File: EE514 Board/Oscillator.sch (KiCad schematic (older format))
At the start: 13 parts

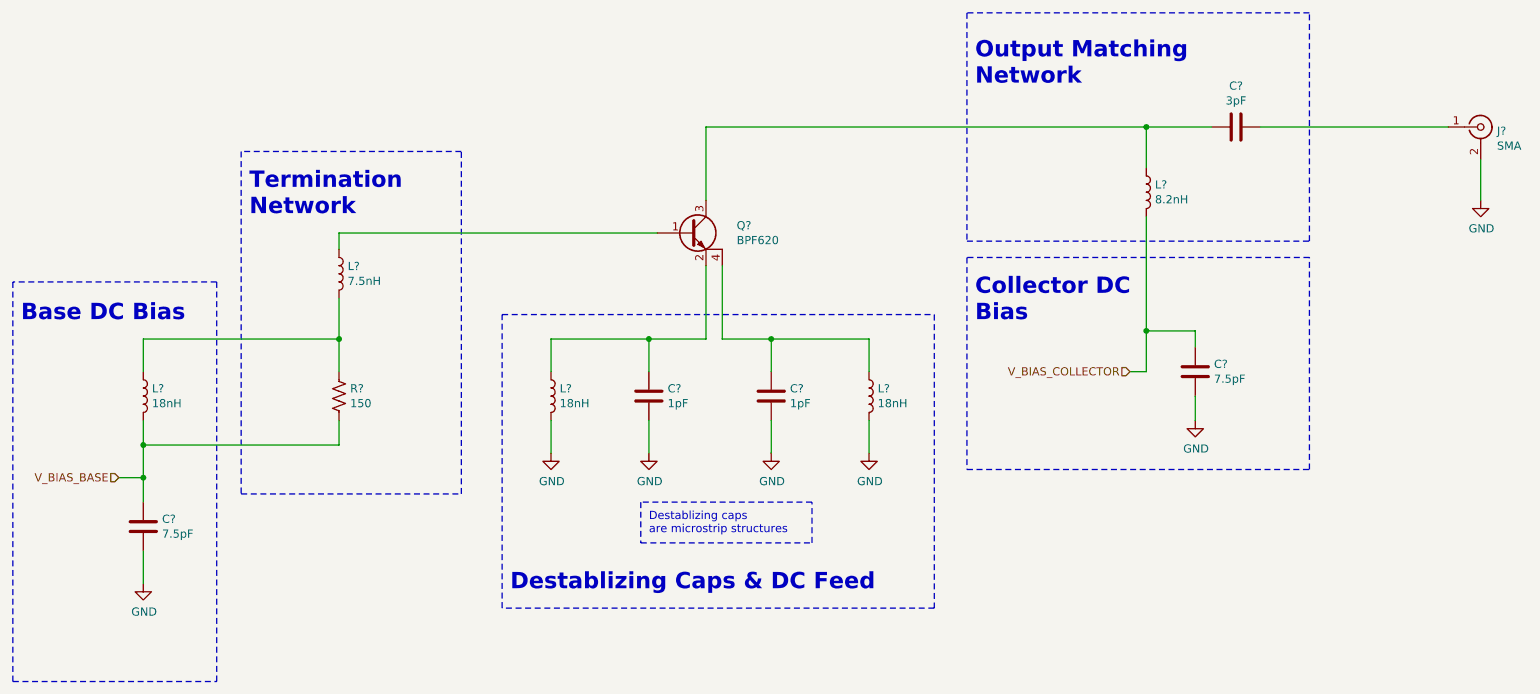
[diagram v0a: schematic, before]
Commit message: Layout finished, updating silkscreen...
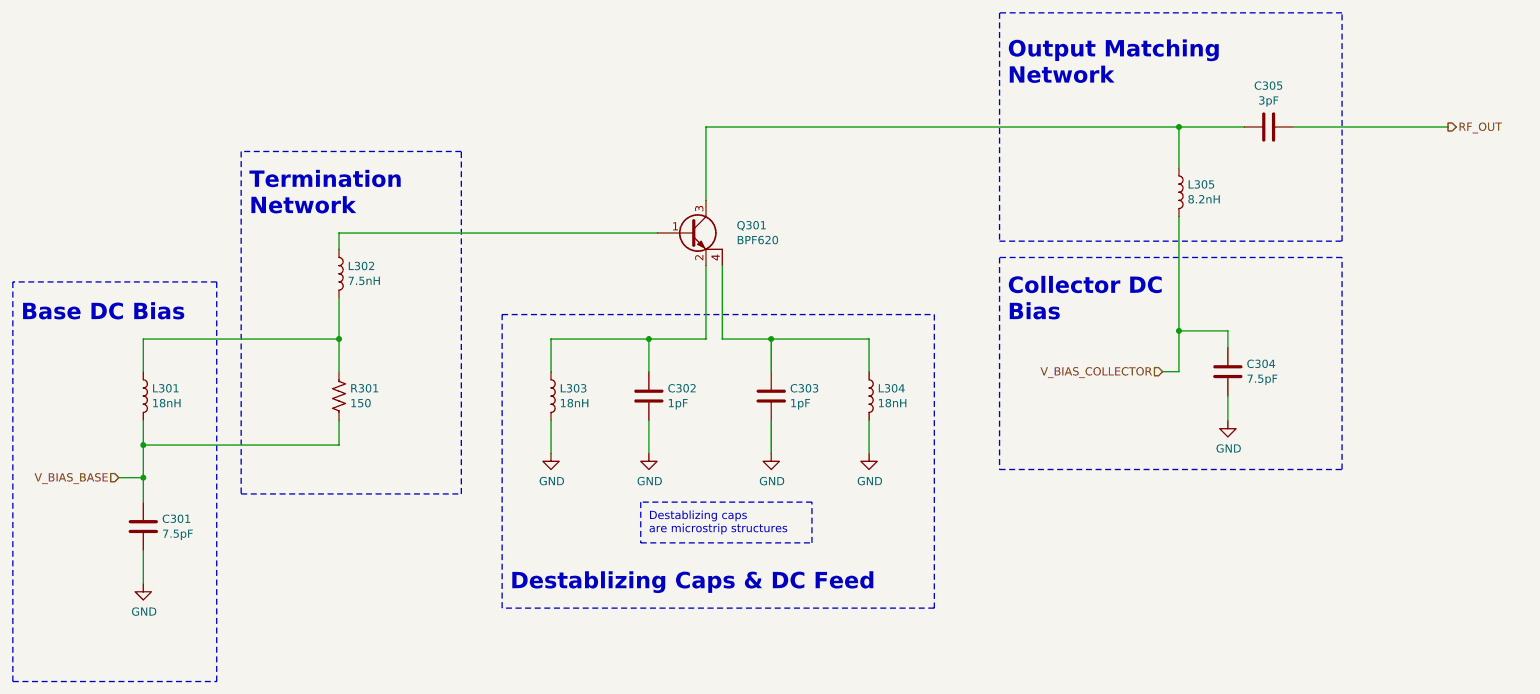
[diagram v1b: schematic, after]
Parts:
- removed J?: SMA, symbol Connector:Conn_Coaxial
- C301, C304, C305: renamed from C?; footprint (none) -> EE514 Board:C_0603_1608Metric_Pad0.98x0.95mm_HandSolder
- C302, C303: renamed from C?; footprint (none) -> EE514 Board:C_1pF_Interdigital
- L301, L302, L303, L304, L305: renamed from L?; footprint (none) -> EE514 Board:L_0603_1608Metric_Pad0.98x0.95mm_HandSolder
- Q301: renamed from Q?; footprint (none) -> EE514 Board:SOT-343_2.0x1.25mm_P1.3mm
- R301: renamed from R?; footprint (none) -> EE514 Board:R_0603_1608Metric_Pad0.98x0.95mm_HandSolder
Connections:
- net RF_OUT: now reaches C305.1
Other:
- moved on the sheet: C304, C305, L305
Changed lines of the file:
@@
 $Descr A4 11693 8268
 encoding utf-8
-Sheet 3 4
+Sheet 3 5
 Title ""
 Date ""
@@
 $EndDescr
 $Comp
-L Device:C C?
+L Device:C C301
 U 1 1 619CBBF5
 P 2250 4900
-F 0 "C?" H 2365 4946 50  0000 L CNN
+F 0 "C301" H 2365 4946 50  0000 L CNN
 F 1 "7.5pF" H 2365 4855 50  0000 L CNN
-F 2 "" H 2288 4750 50  0001 C CNN
+F 2 "EE514 Board:C_0603_1608Metric_Pad0.98x0.95mm_HandSolder" H 2288 4750 50  0001 C CNN
 F 3 "~" H 2250 4900 50  0001 C CNN
 	1    2250 4900
@@
 $EndComp
 $Comp
-L power:GND #PWR?
+L power:GND #PWR0301
 U 1 1 619CC4D1
 P 2250 5250
-F 0 "#PWR?" H 2250 5000 50  0001 C CNN
+F 0 "#PWR0301" H 2250 5000 50  0001 C CNN
 F 1 "GND" H 2255 5077 50  0000 C CNN
 F 2 "" H 2250 5250 50  0001 C CNN
@@
 $EndComp
 $Comp
-L Device:R_US R?
+L Device:R_US R301
 U 1 1 619CCA1F
 P 3450 4100
-F 0 "R?" H 3518 4146 50  0000 L CNN
+F 0 "R301" H 3518 4146 50  0000 L CNN
 F 1 "150" H 3518 4055 50  0000 L CNN
-F 2 "" V 3490 4090 50  0001 C CNN
+F 2 "EE514 Board:R_0603_1608Metric_Pad0.98x0.95mm_HandSolder" V 3490 4090 50  0001 C CNN
 F 3 "~" H 3450 4100 50  0001 C CNN
 	1    3450 4100
@@
 $EndComp
 $Comp
-L EE514_Board:Q_NPN_BECE Q?
+L EE514_Board:Q_NPN_BECE Q301
 U 1 1 619CD2F0
 P 5600 3100
-F 0 "Q?" H 5888 3146 50  0000 L CNN
+F 0 "Q301" H 5888 3146 50  0000 L CNN
 F 1 "BPF620" H 5888 3055 50  0000 L CNN
-F 2 "" H 5800 3200 50  0001 C CNN
+F 2 "EE514 Board:SOT-343_2.0x1.25mm_P1.3mm" H 5800 3200 50  0001 C CNN
 F 3 "~" H 5600 3100 50  0001 C CNN
 	1    5600 3100
@@
 $EndComp
 $Comp
-L Device:L L?
+L Device:L L301
 U 1 1 619CDAD5
 P 2250 4100
-F 0 "L?" H 2303 4146 50  0000 L CNN
+F 0 "L301" H 2303 4146 50  0000 L CNN
 F 1 "18nH" H 2303 4055 50  0000 L CNN
-F 2 "" H 2250 4100 50  0001 C CNN
+F 2 "EE514 Board:L_0603_1608Metric_Pad0.98x0.95mm_HandSolder" H 2250 4100 50  0001 C CNN
 F 3 "~" H 2250 4100 50  0001 C CNN
 	1    2250 4100
@@
 	2250 5250 2250 5050
 $Comp
-L Device:L L?
+L Device:L L302
 U 1 1 619CE6FD
 P 3450 3350
-F 0 "L?" H 3503 3396 50  0000 L CNN
+F 0 "L302" H 3503 3396 50  0000 L CNN
 F 1 "7.5nH" H 3503 3305 50  0000 L CNN
-F 2 "" H 3450 3350 50  0001 C CNN
+F 2 "EE514 Board:L_0603_1608Metric_Pad0.98x0.95mm_HandSolder" H 3450 3350 50  0001 C CNN
 F 3 "~" H 3450 3350 50  0001 C CNN
 	1    3450 3350
@@
 V_BIAS_BASE
 $Comp
-L Device:L L?
+L Device:L L304
 U 1 1 619D273A
 P 6700 4100
-F 0 "L?" H 6753 4146 50  0000 L CNN
+F 0 "L304" H 6753 4146 50  0000 L CNN
 F 1 "18nH" H 6753 4055 50  0000 L CNN
-F 2 "" H 6700 4100 50  0001 C CNN
+F 2 "EE514 Board:L_0603_1608Metric_Pad0.98x0.95mm_HandSolder" H 6700 4100 50  0001 C CNN
 F 3 "~" H 6700 4100 50  0001 C CNN
 	1    6700 4100
@@
 $EndComp
 $Comp
-L power:GND #PWR?
+L power:GND #PWR0304
 U 1 1 619D452E
 P 6100 4450
-F 0 "#PWR?" H 6100 4200 50  0001 C CNN
+F 0 "#PWR0304" H 6100 4200 50  0001 C CNN
 F 1 "GND" H 6105 4277 50  0000 C CNN
 F 2 "" H 6100 4450 50  0001 C CNN
@@
 $EndComp
 $Comp
-L power:GND #PWR?
+L power:GND #PWR0305
 U 1 1 619D47D5
 P 6700 4450
-F 0 "#PWR?" H 6700 4200 50  0001 C CNN
+F 0 "#PWR0305" H 6700 4200 50  0001 C CNN
 F 1 "GND" H 6705 4277 50  0000 C CNN
 F 2 "" H 6700 4450 50  0001 C CNN
@@
 Connection ~ 6100 3750
 $Comp
-L Device:C C?
+L Device:C C302
 U 1 1 619D53B8
 P 5350 4100
-F 0 "C?" H 5465 4146 50  0000 L CNN
+F 0 "C302" H 5465 4146 50  0000 L CNN
 F 1 "1pF" H 5465 4055 50  0000 L CNN
-F 2 "" H 5388 3950 50  0001 C CNN
+F 2 "EE514 Board:C_1pF_Interdigital" H 5388 3950 50  0001 C CNN
 F 3 "~" H 5350 4100 50  0001 C CNN
 	1    5350 4100
@@
 $EndComp
 $Comp
-L Device:L L?
+L Device:L L303
 U 1 1 619D65CF
 P 4750 4100
-F 0 "L?" H 4803 4146 50  0000 L CNN
+F 0 "L303" H 4803 4146 50  0000 L CNN
 F 1 "18nH" H 4803 4055 50  0000 L CNN
-F 2 "" H 4750 4100 50  0001 C CNN
+F 2 "EE514 Board:L_0603_1608Metric_Pad0.98x0.95mm_HandSolder" H 4750 4100 50  0001 C CNN
 F 3 "~" H 4750 4100 50  0001 C CNN
 	1    4750 4100
@@
 $EndComp
 $Comp
-L power:GND #PWR?
+L power:GND #PWR0302
 U 1 1 619D7793
 P 4750 4450
-F 0 "#PWR?" H 4750 4200 50  0001 C CNN
+F 0 "#PWR0302" H 4750 4200 50  0001 C CNN
 F 1 "GND" H 4755 4277 50  0000 C CNN
 F 2 "" H 4750 4450 50  0001 C CNN
@@
 $EndComp
 $Comp
-L power:GND #PWR?
+L power:GND #PWR0303
 U 1 1 619D7799
 P 5350 4450
-F 0 "#PWR?" H 5350 4200 50  0001 C CNN
+F 0 "#PWR0303" H 5350 4200 50  0001 C CNN
 F 1 "GND" H 5355 4277 50  0000 C CNN
 F 2 "" H 5350 4450 50  0001 C CNN
@@
 L Device:L L?
 U 1 1 619E13A4
-P 8400 2850
+P 8600 2850
 AR Path="/6196B9B8/619E13A4" Ref="L?"  Part="1"
-AR Path="/619CBABE/619E13A4" Ref="L?"  Part="1"
-F 0 "L?" H 8453 2896 50  0000 L CNN
-F 1 "8.2nH" H 8453 2805 50  0000 L CNN
-F 2 "" H 8400 2850 50  0001 C CNN
-F 3 "~" H 8400 2850 50  0001 C CNN
-	1    8400 2850
-	1    0    0    -1
-$EndComp
-Wire Wire Line
-	8400 3700 8400 3000
-Wire Wire Line
-	8700 3800 8700 3700
-Wire Wire Line
-	8700 3700 8400 3700
+AR Path="/619CBABE/619E13A4" Ref="L305"  Part="1"
+F 0 "L305" H 8653 2896 50  0000 L CNN
+F 1 "8.2nH" H 8653 2805 50  0000 L CNN
+F 2 "EE514 Board:L_0603_1608Metric_Pad0.98x0.95mm_HandSolder" H 8600 2850 50  0001 C CNN
+F 3 "~" H 8600 2850 50  0001 C CNN
+	1    8600 2850
+	1    0    0    -1
+$EndComp
+Wire Wire Line
+	8600 3700 8600 3000
+Wire Wire Line
+	8900 3800 8900 3700
+Wire Wire Line
+	8900 3700 8600 3700
 $Comp
 L power:GND #PWR?
 U 1 1 619E13AD
-P 8700 4250
+P 8900 4250
 AR Path="/6196B9B8/619E13AD" Ref="#PWR?"  Part="1"
-AR Path="/619CBABE/619E13AD" Ref="#PWR?"  Part="1"
-F 0 "#PWR?" H 8700 4000 50  0001 C CNN
-F 1 "GND" H 8705 4077 50  0000 C CNN
-F 2 "" H 8700 4250 50  0001 C CNN
-F 3 "" H 8700 4250 50  0001 C CNN
-	1    8700 4250
-	1    0    0    -1
-$EndComp
-Wire Wire Line
-	8700 4250 8700 4100
-Wire Wire Line
-	8400 3700 8400 3950
-Wire Wire Line
-	8400 3950 8300 3950
-Connection ~ 8400 3700
-Text HLabel 8300 3950 0    50   Input ~ 0
+AR Path="/619CBABE/619E13AD" Ref="#PWR0306"  Part="1"
+F 0 "#PWR0306" H 8900 4000 50  0001 C CNN
+F 1 "GND" H 8905 4077 50  0000 C CNN
+F 2 "" H 8900 4250 50  0001 C CNN
+F 3 "" H 8900 4250 50  0001 C CNN
+	1    8900 4250
+	1    0    0    -1
+$EndComp
+Wire Wire Line
+	8900 4250 8900 4100
+Wire Wire Line
+	8600 3700 8600 3950
+Wire Wire Line
+	8600 3950 8500 3950
+Connection ~ 8600 3700
+Text HLabel 8500 3950 0    50   Input ~ 0
 V_BIAS_COLLECTOR
 Wire Wire Line
-	8400 2450 8400 2700
+	8600 2450 8600 2700
 $Comp
 L Device:C C?
 U 1 1 619E13B9
-P 8950 2450
+P 9150 2450
 AR Path="/6196B9B8/619E13B9" Ref="C?"  Part="1"
-AR Path="/619CBABE/619E13B9" Ref="C?"  Part="1"
-F 0 "C?" V 8698 2450 50  0000 C CNN
-F 1 "3pF" V 8789 2450 50  0000 C CNN
-F 2 "" H 8988 2300 50  0001 C CNN
-F 3 "~" H 8950 2450 50  0001 C CNN
-	1    8950 2450
+AR Path="/619CBABE/619E13B9" Ref="C305"  Part="1"
+F 0 "C305" V 8898 2450 50  0000 C CNN
+F 1 "3pF" V 8989 2450 50  0000 C CNN
+F 2 "EE514 Board:C_0603_1608Metric_Pad0.98x0.95mm_HandSolder" H 9188 2300 50  0001 C CNN
+F 3 "~" H 9150 2450 50  0001 C CNN
+	1    9150 2450
 	0    1    1    0
 $EndComp
 Wire Wire Line
-	8400 2450 8800 2450
-Connection ~ 8400 2450
-Wire Notes Line
-	7300 1750 7300 3150
-Wire Notes Line
-	7300 3150 9400 3150
-Wire Notes Line
-	9400 3150 9400 1750
-Wire Notes Line
-	9400 1750 7300 1750
-Text Notes 7350 2200 0    100  ~ 20
+	8600 2450 9000 2450
+Connection ~ 8600 2450
+Wire Notes Line
+	7500 1750 7500 3150
+Wire Notes Line
+	7500 3150 9600 3150
+Wire Notes Line
+	9600 3150 9600 1750
+Wire Notes Line
+	9600 1750 7500 1750
+Text Notes 7550 2200 0    100  ~ 20
 Output Matching \nNetwork\n
-Text Notes 7350 3650 0    100  ~ 20
+Text Notes 7550 3650 0    100  ~ 20
 Collector DC \nBias
 Wire Notes Line
-	7300 4550 9400 4550
-Wire Notes Line
-	9400 4550 9400 3250
-Wire Notes Line
-	9400 3250 7300 3250
-Wire Notes Line
-	7300 3250 7300 4550
+	7500 4550 9600 4550
+Wire Notes Line
+	9600 4550 9600 3250
+Wire Notes Line
+	9600 3250 7500 3250
+Wire Notes Line
+	7500 3250 7500 4550
 $Comp
 L Device:C C?
 U 1 1 619E13CC
-P 8700 3950
+P 8900 3950
 AR Path="/6196B9B8/619E13CC" Ref="C?"  Part="1"
-AR Path="/619CBABE/619E13CC" Ref="C?"  Part="1"
-F 0 "C?" H 8815 3996 50  0000 L CNN
-F 1 "7.5pF" H 8815 3905 50  0000 L CNN
-F 2 "" H 8738 3800 50  0001 C CNN
-F 3 "~" H 8700 3950 50  0001 C CNN
-	1    8700 3950
+AR Path="/619CBABE/619E13CC" Ref="C304"  Part="1"
+F 0 "C304" H 9015 3996 50  0000 L CNN
+F 1 "7.5pF" H 9015 3905 50  0000 L CNN
+F 2 "EE514 Board:C_0603_1608Metric_Pad0.98x0.95mm_HandSolder" H 8938 3800 50  0001 C CNN
+F 3 "~" H 8900 3950 50  0001 C CNN
+	1    8900 3950
 	1    0    0    -1
 $EndComp
@@
 	5700 2900 5700 2450
 Wire Wire Line
-	5700 2450 8400 2450
-$Comp
-L Connector:Conn_Coaxial J?
-U 1 1 619E6B6A
-P 10450 2450
-AR Path="/6196B9B8/619E6B6A" Ref="J?"  Part="1"
-AR Path="/619CBABE/619E6B6A" Ref="J?"  Part="1"
-F 0 "J?" H 10550 2425 50  0000 L CNN
-F 1 "SMA" H 10550 2334 50  0000 L CNN
-F 2 "" H 10450 2450 50  0001 C CNN
-F 3 " ~" H 10450 2450 50  0001 C CNN
-	1    10450 2450
-	1    0    0    -1
-$EndComp
-Wire Wire Line
-	10450 2650 10450 2900
-$Comp
-L power:GND #PWR?
-U 1 1 619E6B72
-P 10450 2900
-AR Path="/6196B9B8/619E6B72" Ref="#PWR?"  Part="1"
-AR Path="/619CBABE/619E6B72" Ref="#PWR?"  Part="1"
-F 0 "#PWR?" H 10450 2650 50  0001 C CNN
-F 1 "GND" H 10455 2727 50  0000 C CNN
-F 2 "" H 10450 2900 50  0001 C CNN
-F 3 "" H 10450 2900 50  0001 C CNN
-	1    10450 2900
-	1    0    0    -1
-$EndComp
-Wire Wire Line
-	9100 2450 10250 2450
-$Comp
-L Device:C C?
+	5700 2450 8600 2450
+Wire Wire Line
+	9300 2450 10250 2450
+$Comp
+L Device:C C303
 U 1 1 619D33FC
 P 6100 4100
-F 0 "C?" H 6215 4146 50  0000 L CNN
+F 0 "C303" H 6215 4146 50  0000 L CNN
 F 1 "1pF" H 6215 4055 50  0000 L CNN
-F 2 "" H 6138 3950 50  0001 C CNN
+F 2 "EE514 Board:C_1pF_Interdigital" H 6138 3950 50  0001 C CNN
 F 3 "~" H 6100 4100 50  0001 C CNN
 	1    6100 4100
@@
 Wire Wire Line
 	2250 4400 2250 4600
+Text HLabel 10250 2450 2    50   Output ~ 0
+RF_OUT
 $EndSCHEMATC
